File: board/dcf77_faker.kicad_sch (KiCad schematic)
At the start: 42 parts, among them J1 Barrel_Jack, J2 DBG, J3 ANT, J4 LCD_I2C, SW1 RST, U1 NCP1117ST33T3G, U2 ATSAML21G18B-AUT, X1 32.768kHz, X2 31MHz

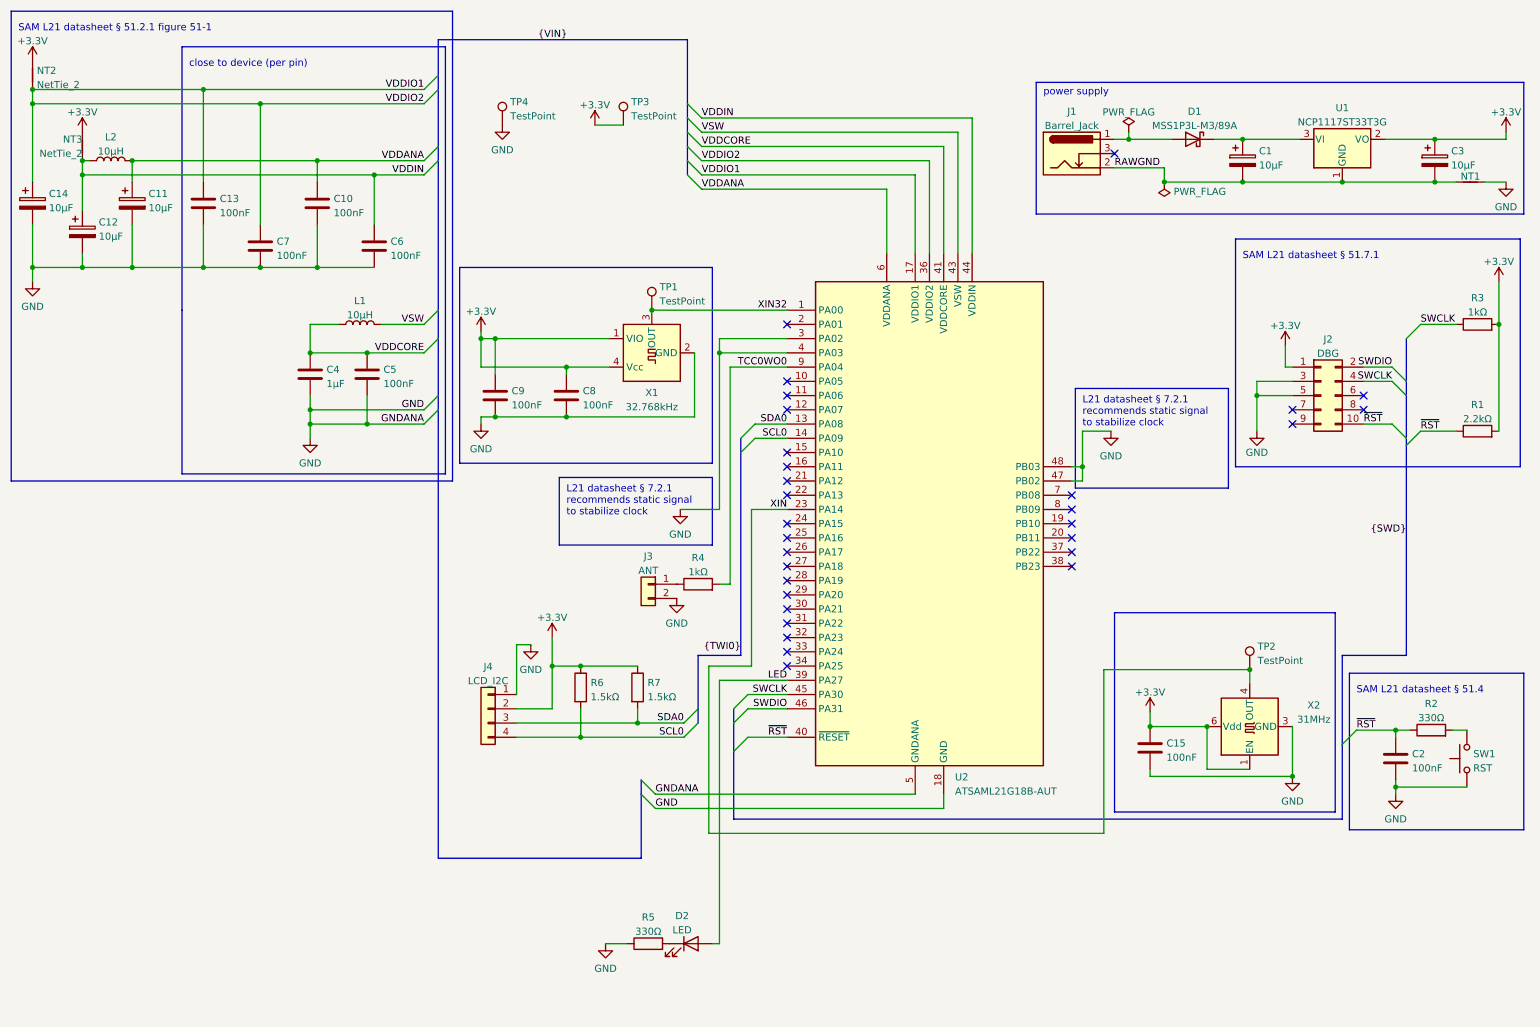
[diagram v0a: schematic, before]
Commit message: board: align schematic to grid
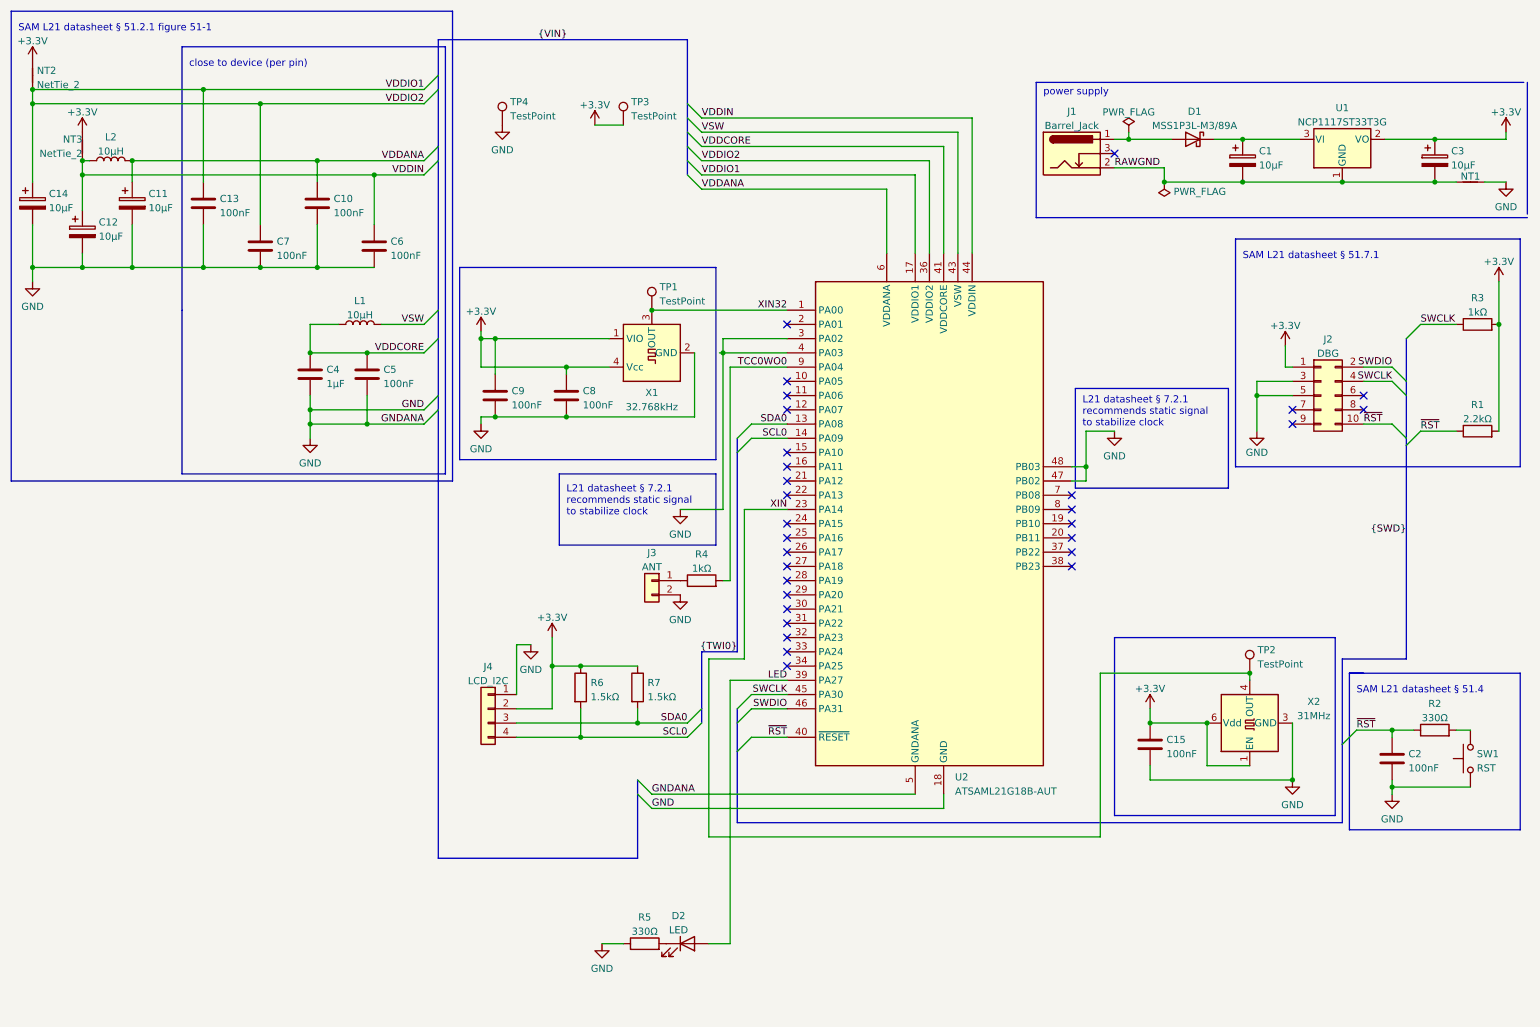
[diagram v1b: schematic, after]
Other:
- moved on the sheet: C15, C2, D2, J3, R2, R4, R5, SW1, TP2, X2

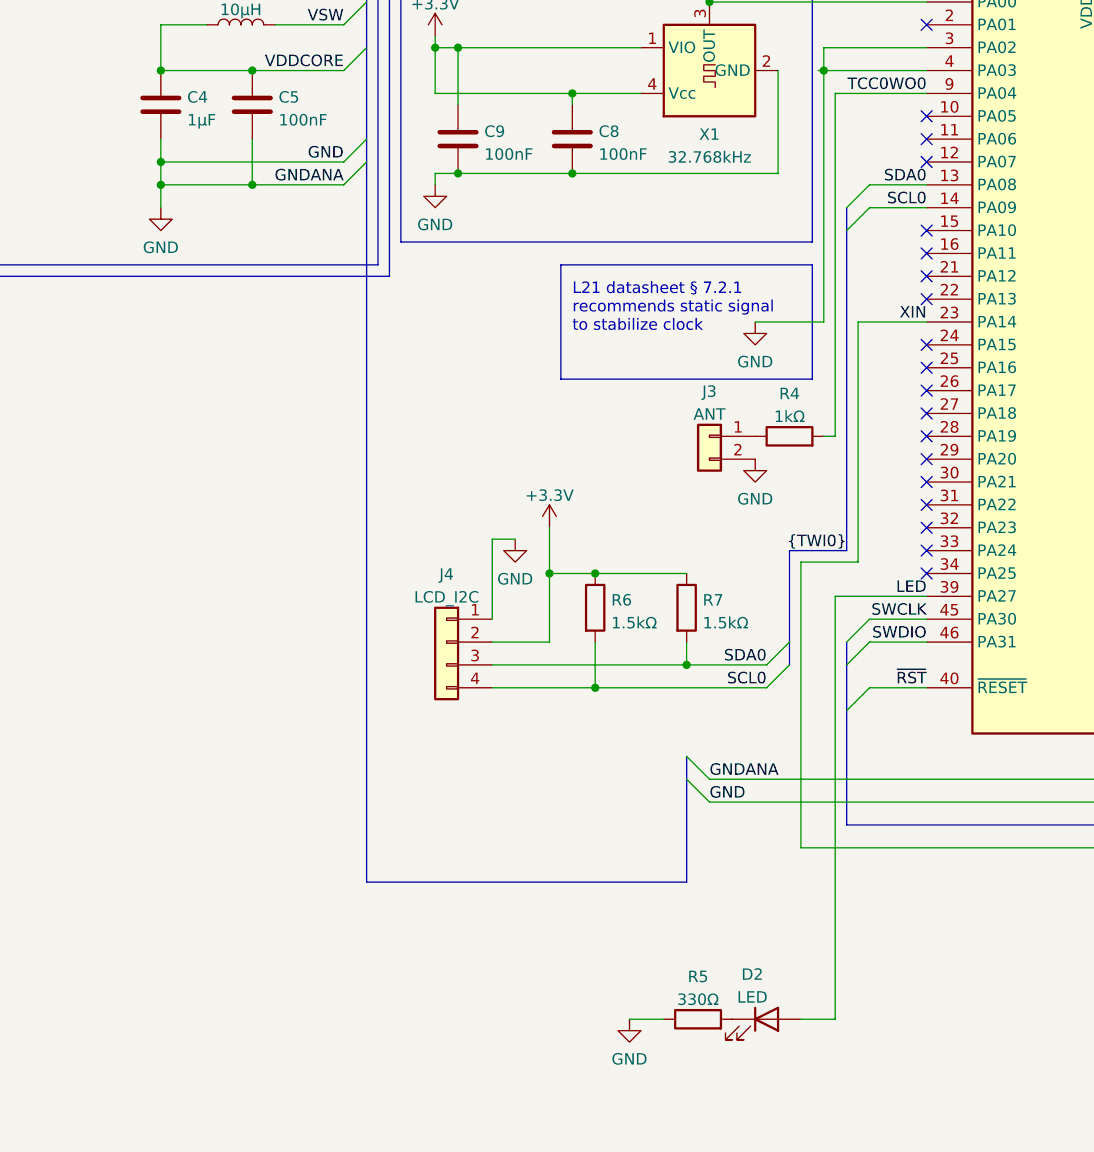
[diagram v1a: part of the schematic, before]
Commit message: board: add buttons to set hour/minute or reset second
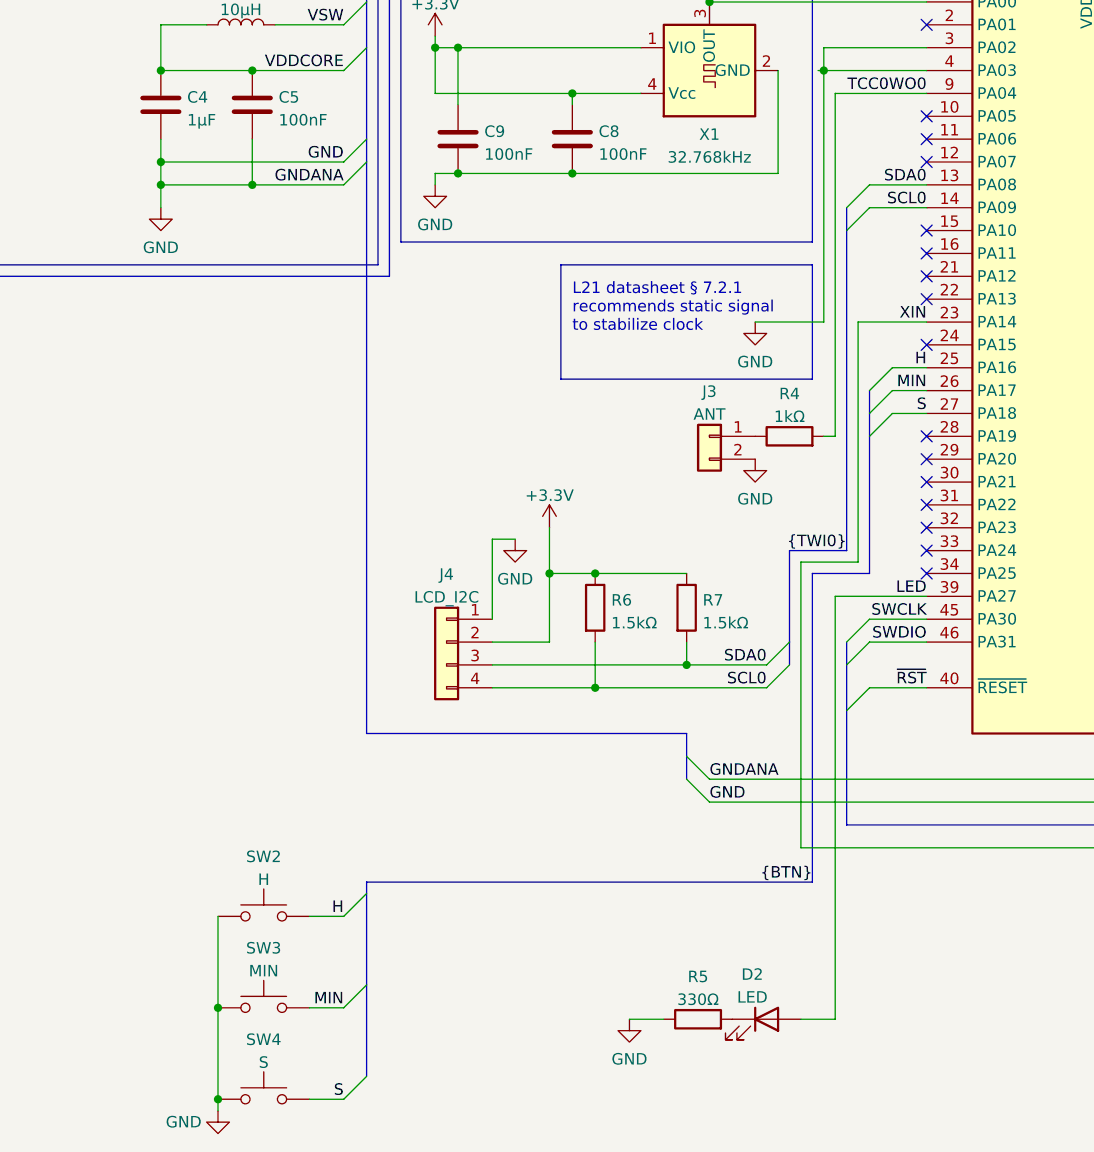
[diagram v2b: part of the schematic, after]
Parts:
- added SW2: H, Button_Switch_SMD_Side:Shou_Han_TS24CA, symbol Switch:SW_Push
- added SW3: MIN, Button_Switch_SMD_Side:Shou_Han_TS24CA, symbol Switch:SW_Push
- added SW4: S, Button_Switch_SMD_Side:Shou_Han_TS24CA, symbol Switch:SW_Push
- SW1: footprint Button_Switch_SMD_Custom:Shou_Han_TS24CA -> Button_Switch_SMD_Side:Shou_Han_TS24CA
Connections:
- net GND: now also SW2.1, SW3.1, SW4.1
- net H: now reaches U2.25 (PA16)
- net H: now also SW2.2
- net MIN: now reaches U2.26 (PA17)
- net MIN: now also SW3.2
- net S: now reaches U2.27 (PA18)
- net S: now also SW4.2
- no-connect marks 30 -> 27

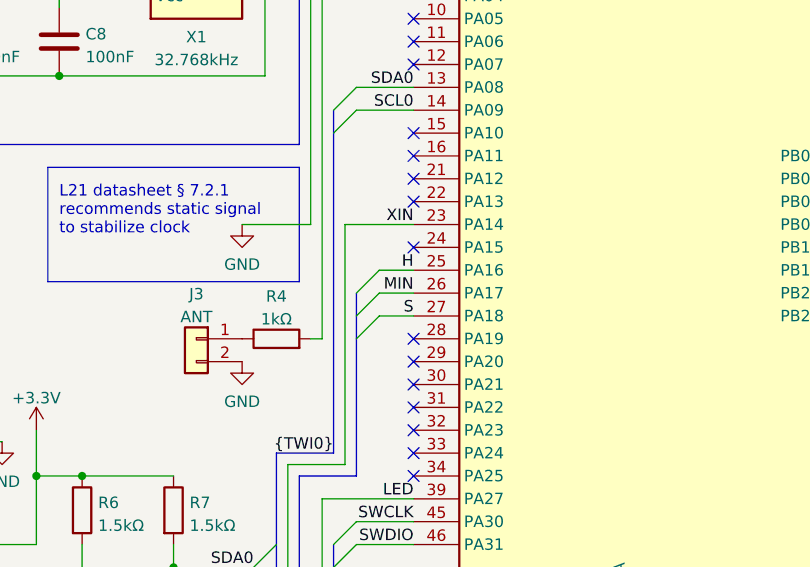
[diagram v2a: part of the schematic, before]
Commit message: board: reorder HMS button pins
this increases planarity of the PCB tracks
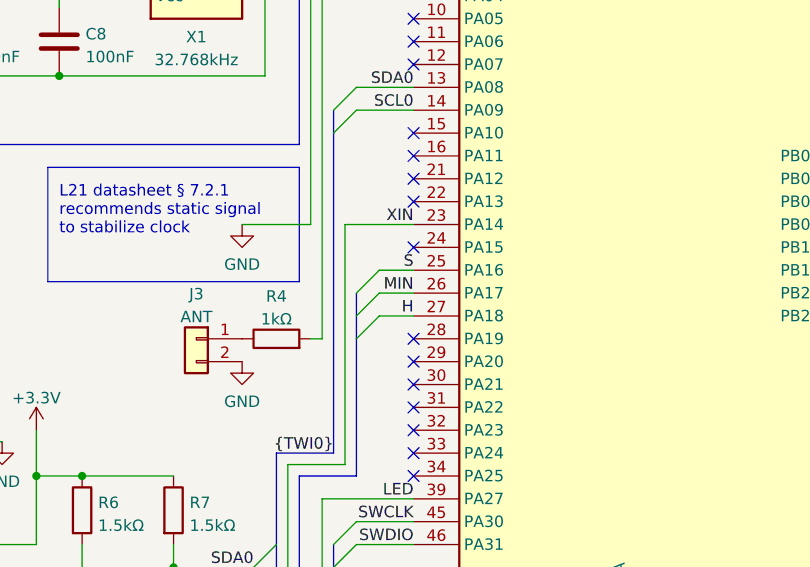
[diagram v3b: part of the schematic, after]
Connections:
- net H: now also U2.27 (PA18); no longer U2.25 (PA16)
- net S: now also U2.25 (PA16); no longer U2.27 (PA18)
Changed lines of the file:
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@@
     (effects (font (size 1.27 1.27)) (justify right bottom))
   )
-  (label "H" (at 152.4 109.22 180)
+  (label "S" (at 152.4 109.22 180)
     (effects (font (size 1.27 1.27)) (justify right bottom))
   )
@@
     (effects (font (size 1.27 1.27)) (justify left bottom))
   )
-  (label "S" (at 152.4 114.3 180)
+  (label "H" (at 152.4 114.3 180)
     (effects (font (size 1.27 1.27)) (justify right bottom))
   )

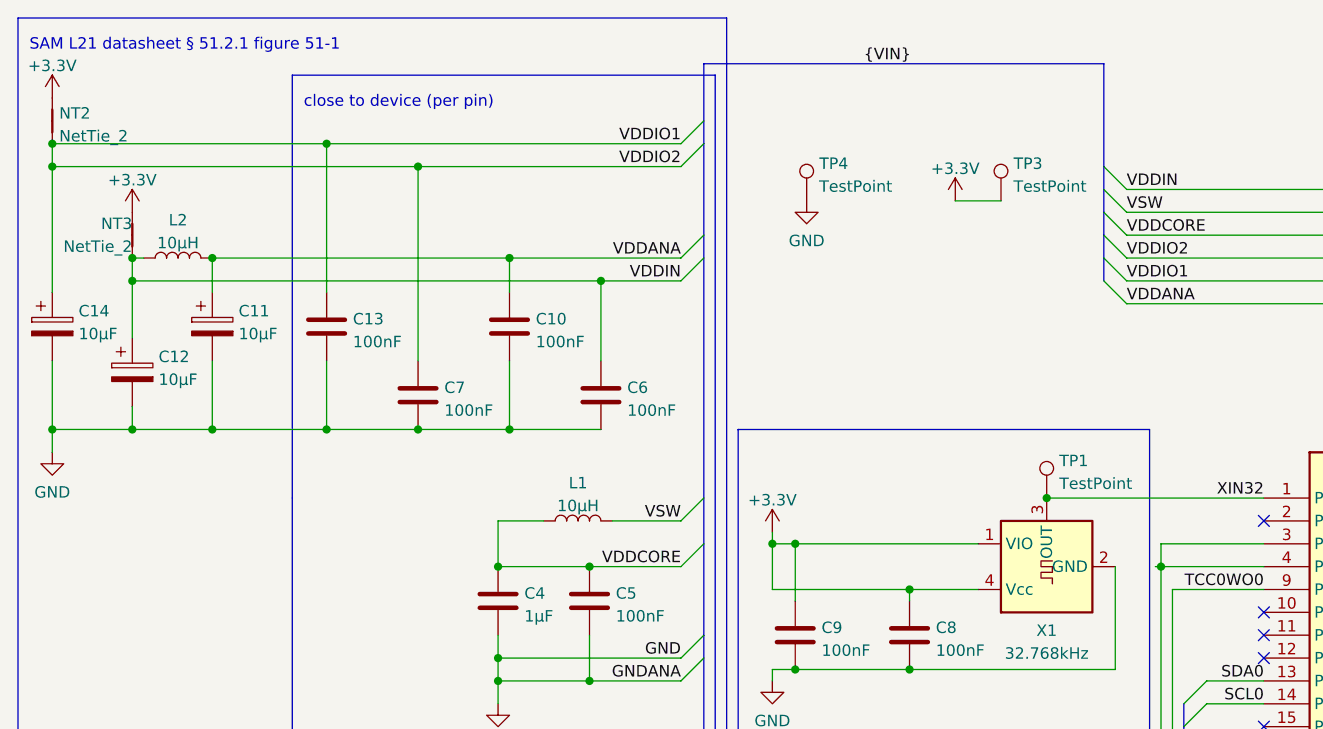
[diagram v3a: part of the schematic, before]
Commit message: board: force VDDIO1 and VDDIO2 to be independent nets
otherwise the name of the common net will keep changing
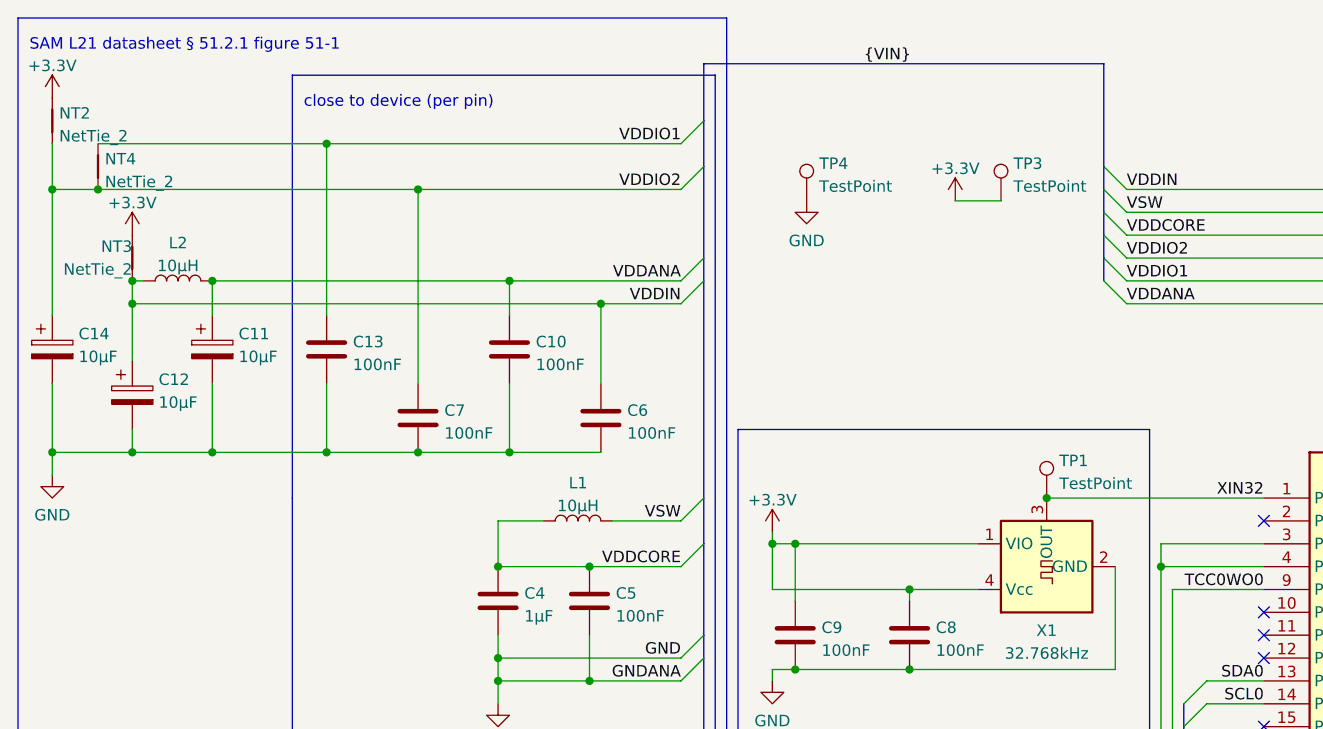
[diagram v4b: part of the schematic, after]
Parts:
- added NT4: NetTie_2, NetTie:NetTie-2_SMD_Pad0.5mm, symbol Device:NetTie_2
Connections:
- net VDDIO1: now also NT4.2; no longer C14.1, C7.1, NT2.1, U2.36 (VDDIO2)
- new net VDDIO2: C14.1, C7.1, NT2.1, NT4.1, U2.36 (VDDIO2)
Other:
- moved on the sheet: C10, C11, C12, C13, C14, C6, C7, L2, NT3
